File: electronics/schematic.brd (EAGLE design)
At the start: 100 x 80 mm, 3 parts, among them Q1 MC-405

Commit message: Board getting close. Before switching Around
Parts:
- removed SV1: (no value), con-lstb:MA06-1
- added GND, GND2, LED+, LED-, RST, RXD, TEST, TXD, VCC, VCC2: TPTP15R, testpad:TP15R
- added Q3: SST201, transistor-fet:SOT23
- moved Q1 1.91 mm to (22.9, 20.3)
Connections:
- removed net VSS: SV1.2, U$1.4
- new net GND: GND.TP, Q3.2, U$1.4
- new net N$4: LED-.TP, Q3.1
- net LED: now also Q3.3
- net N$1: now also Q1.P$6; no longer Q1.P$3
- net N$2: now also Q1.P$3; no longer Q1.P$6
- net RST: now also RST.TP; no longer SV1.1
- net RXD: now also RXD.TP; no longer SV1.6
- net TEST: now also TEST.TP; no longer SV1.4
- net TXD: now also TXD.TP; no longer SV1.5
- net VCC: now also LED+.TP, VCC.TP; no longer SV1.3
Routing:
- net VCC: track 7.39 -> 28.1 mm
- net VSS: track 10.4 -> 0.00 mm
- net GND: track 0.00 -> 8.23 mm
- net N$4: track 0.00 -> 4.15 mm
- net N$1: track 12.9 -> 11.4 mm
- net TXD: track 11.2 -> 9.93 mm
- net TEST: track 12.5 -> 11.2 mm
- net RST: track 12.9 -> 11.7 mm
- net RXD: track 11.7 -> 12.9 mm
- net N$2: track 9.47 -> 10.6 mm

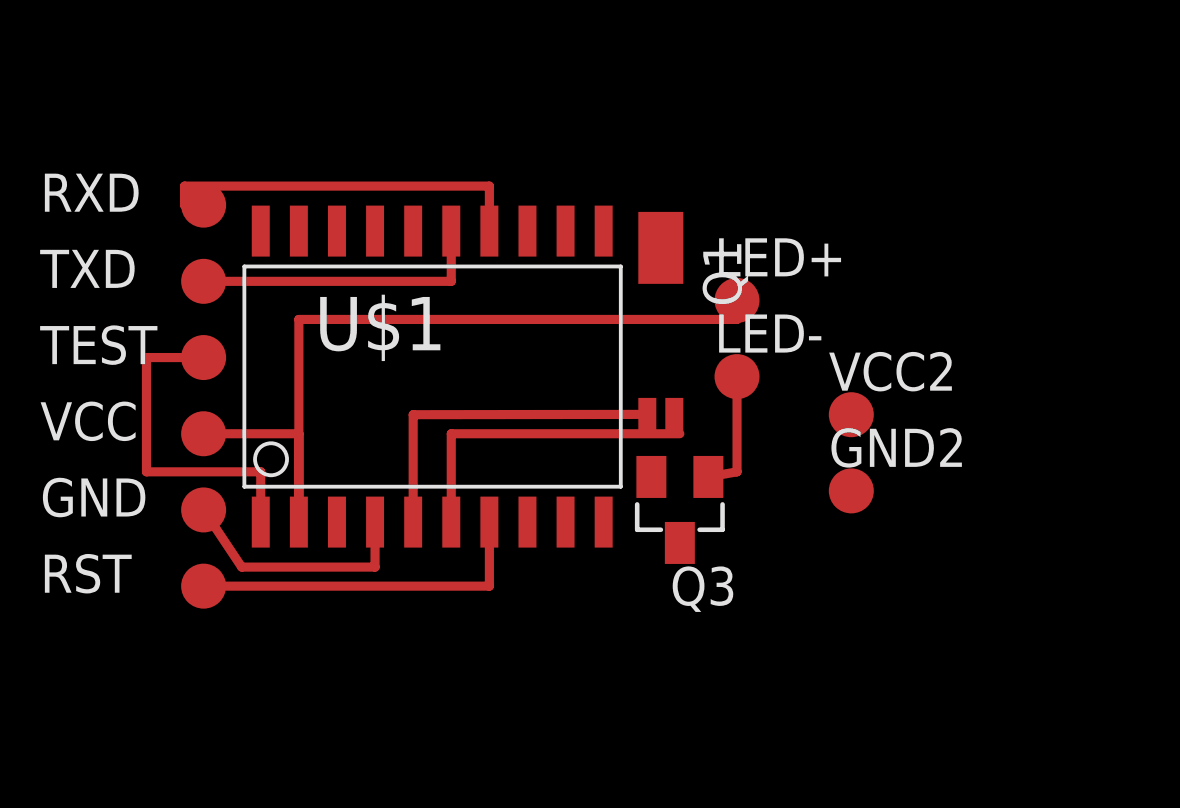
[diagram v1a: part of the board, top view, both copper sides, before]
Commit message: Finished 1 layer design
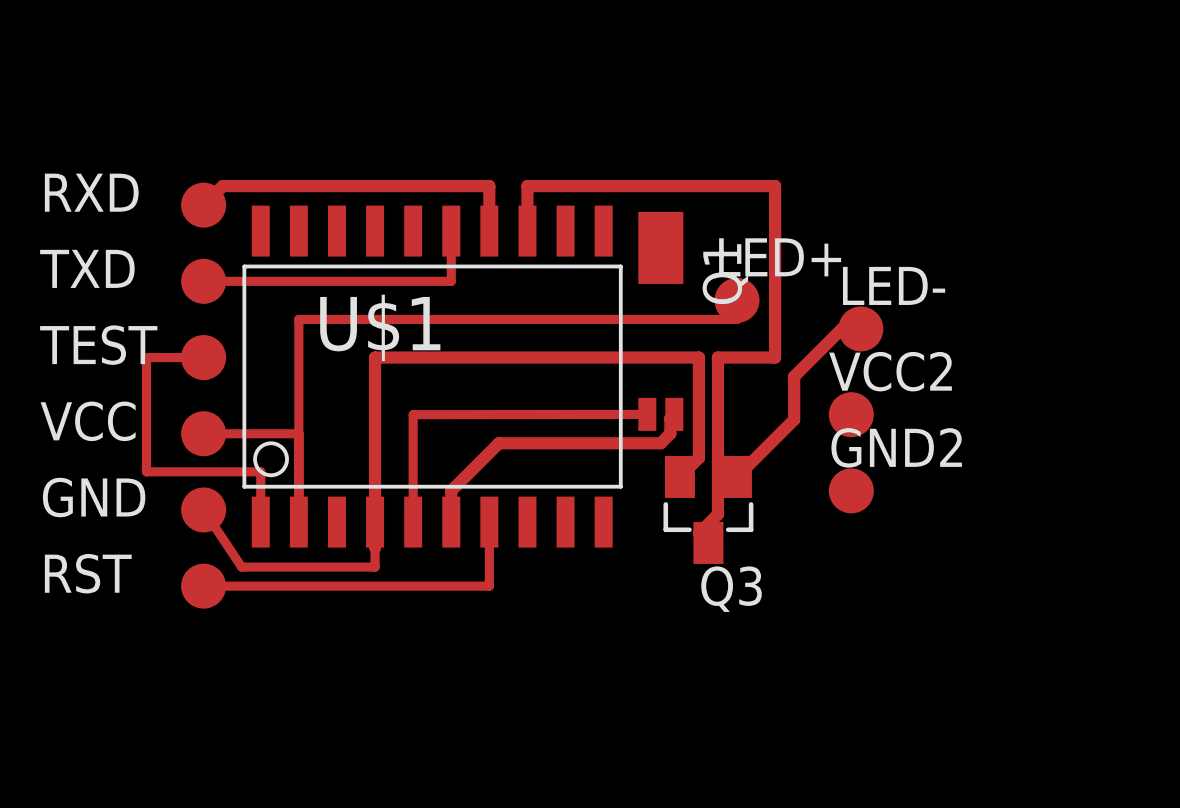
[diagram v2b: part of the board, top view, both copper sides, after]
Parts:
- moved LED- 4.42 mm to (29.5, 19.4)
- moved Q3 0.95 mm to (24.4, 13.3)
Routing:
- net LED: track 0.00 -> 23.9 mm
- net GND: track 8.23 -> 29.6 mm
- net N$4: track 4.15 -> 7.02 mm
- net RXD: track 12.9 -> 11.3 mm
- net N$2: track 10.6 -> 9.83 mm
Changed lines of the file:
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@@
 </element>
 <element name="U$1" library="TI_MSP430_v16" package="DW20" value="F21X1---DW20" x="15.24" y="17.78"/>
-<element name="Q3" library="transistor-fet" package="SOT23" value="SST201" x="23.495" y="13.335" rot="R180"/>
+<element name="Q3" library="transistor-fet" package="SOT23" value="SST201" x="24.4475" y="13.335" rot="R180"/>
 <element name="RXD" library="testpad" package="TP15R" value="TPTP15R" x="7.62" y="23.495" smashed="yes">
 <attribute name="TP_SIGNAL_NAME" value="" x="7.62" y="20.955" size="1" layer="37"/>
@@
 <attribute name="TP_SIGNAL_NAME" value="" x="25.4" y="20.32" size="1.778" layer="27" display="off"/>
 </element>
-<element name="LED-" library="testpad" package="TP15R" value="TPTP15R" x="25.4" y="17.78">
-<attribute name="TP_SIGNAL_NAME" value="" x="25.4" y="17.78" size="1.778" layer="27" display="off"/>
+<element name="LED-" library="testpad" package="TP15R" value="TPTP15R" x="29.5275" y="19.3675">
+<attribute name="TP_SIGNAL_NAME" value="" x="29.5275" y="19.3675" size="1.778" layer="27" display="off"/>
 </element>
 <element name="VCC2" library="testpad" package="TP15R" value="TPTP15R" x="29.21" y="16.51">
@@
 <contactref element="U$1" pad="6"/>
 <contactref element="Q1" pad="P$3"/>
-<wire x1="15.875" y1="12.93" x2="15.875" y2="15.875" width="0.3048" layer="1"/>
-<wire x1="15.875" y1="15.875" x2="23.495" y2="15.875" width="0.3048" layer="1"/>
-<wire x1="23.495" y1="15.875" x2="23.31" y2="16.52" width="0" layer="19" extent="1-16"/>
+<wire x1="23.31" y1="16.52" x2="23.1775" y2="16.3875" width="0.4064" layer="1"/>
+<wire x1="23.1775" y1="16.3875" x2="23.1775" y2="15.875" width="0.4064" layer="1"/>
+<wire x1="23.1775" y1="15.875" x2="22.86" y2="15.5575" width="0.4064" layer="1"/>
+<wire x1="22.86" y1="15.5575" x2="17.4625" y2="15.5575" width="0.4064" layer="1"/>
+<wire x1="17.4625" y1="15.5575" x2="15.875" y2="13.97" width="0.4064" layer="1"/>
+<wire x1="15.875" y1="13.97" x2="15.875" y2="12.93" width="0.4064" layer="1"/>
 </signal>
 <signal name="TEST">
@@
 <signal name="RXD">
 <contactref element="U$1" pad="14"/>
-<wire x1="17.145" y1="24.13" x2="17.145" y2="22.63" width="0" layer="19" extent="1-16"/>
 <contactref element="RXD" pad="TP"/>
-<wire x1="7.62" y1="23.495" x2="6.985" y2="23.495" width="0.3048" layer="1"/>
-<wire x1="6.985" y1="23.495" x2="6.985" y2="24.13" width="0.3048" layer="1"/>
-<wire x1="6.985" y1="24.13" x2="17.145" y2="24.13" width="0.3048" layer="1"/>
-<wire x1="17.145" y1="24.13" x2="17.145" y2="22.63" width="0.3048" layer="1"/>
+<wire x1="7.62" y1="23.495" x2="8.255" y2="24.13" width="0.4064" layer="1"/>
+<wire x1="8.255" y1="24.13" x2="17.145" y2="24.13" width="0.4064" layer="1"/>
+<wire x1="17.145" y1="24.13" x2="17.145" y2="22.63" width="0.4064" layer="1"/>
 </signal>
 <signal name="LED">
 <contactref element="U$1" pad="13"/>
 <contactref element="Q3" pad="3"/>
-<wire x1="23.495" y1="12.235" x2="18.415" y2="22.63" width="0" layer="19" extent="1-1"/>
+<wire x1="24.4475" y1="12.235" x2="24.13" y2="12.5525" width="0.4064" layer="1"/>
+<wire x1="26.67" y1="18.415" x2="26.67" y2="24.13" width="0.4064" layer="1"/>
+<wire x1="26.67" y1="24.13" x2="18.415" y2="24.13" width="0.4064" layer="1"/>
+<wire x1="18.415" y1="24.13" x2="18.415" y2="22.63" width="0.4064" layer="1"/>
+<wire x1="24.13" y1="12.5525" x2="24.765" y2="13.1875" width="0.4064" layer="1"/>
+<wire x1="24.765" y1="13.1875" x2="24.765" y2="18.415" width="0.4064" layer="1"/>
+<wire x1="24.765" y1="18.415" x2="26.67" y2="18.415" width="0.4064" layer="1"/>
 </signal>
 <signal name="GND">
@@
 <wire x1="7.62" y1="13.335" x2="8.89" y2="11.43" width="0.3048" layer="1"/>
 <wire x1="8.89" y1="11.43" x2="13.335" y2="11.43" width="0.3048" layer="1"/>
-<wire x1="13.335" y1="11.43" x2="13.335" y2="12.93" width="0.3048" layer="1"/>
-<wire x1="13.335" y1="12.93" x2="22.545" y2="14.435" width="0" layer="19" extent="1-1"/>
+<wire x1="13.335" y1="11.43" x2="13.335" y2="12.065" width="0.3048" layer="1"/>
+<wire x1="13.335" y1="12.065" x2="13.335" y2="12.93" width="0.3048" layer="1"/>
+<wire x1="23.4975" y1="14.435" x2="24.13" y2="15.0675" width="0.4064" layer="1"/>
+<wire x1="24.13" y1="15.0675" x2="24.13" y2="18.415" width="0.4064" layer="1"/>
+<wire x1="24.13" y1="18.415" x2="13.335" y2="18.415" width="0.4064" layer="1"/>
+<wire x1="13.335" y1="18.415" x2="13.335" y2="12.065" width="0.4064" layer="1"/>
 </signal>
 <signal name="N$4">
 <contactref element="Q3" pad="1"/>
 <contactref element="LED-" pad="TP"/>
-<wire x1="25.4" y1="17.78" x2="25.4" y2="14.605" width="0.3048" layer="1"/>
-<wire x1="25.4" y1="14.605" x2="24.445" y2="14.435" width="0.3048" layer="1"/>
+<wire x1="25.3975" y1="14.435" x2="27.305" y2="16.3425" width="0.4064" layer="1"/>
+<wire x1="27.305" y1="16.3425" x2="27.305" y2="17.78" width="0.4064" layer="1"/>
+<wire x1="27.305" y1="17.78" x2="28.8925" y2="19.3675" width="0.4064" layer="1"/>
+<wire x1="28.8925" y1="19.3675" x2="29.5275" y2="19.3675" width="0.4064" layer="1"/>
 </signal>
 </signals>

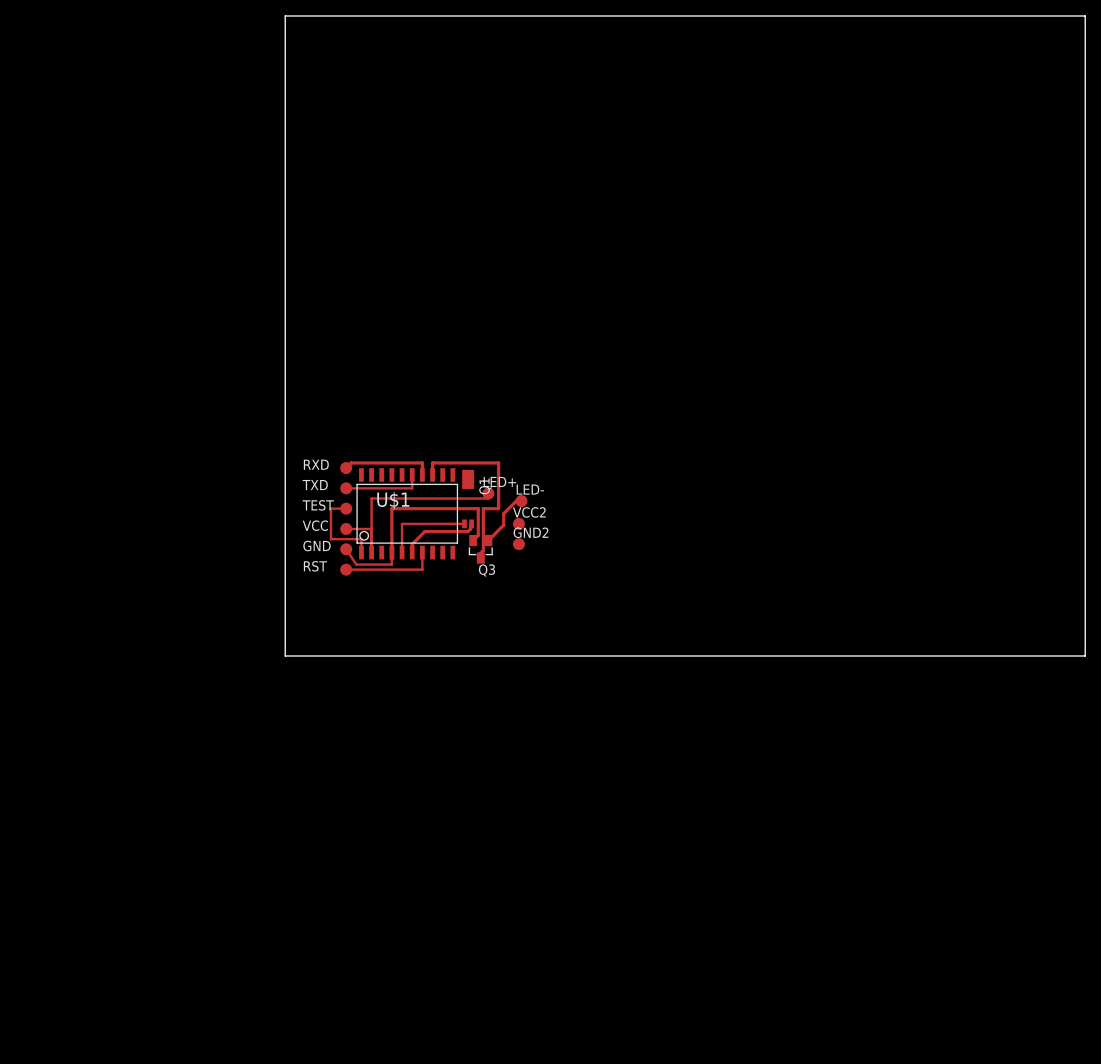
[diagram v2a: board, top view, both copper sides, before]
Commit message: Finished two layer design
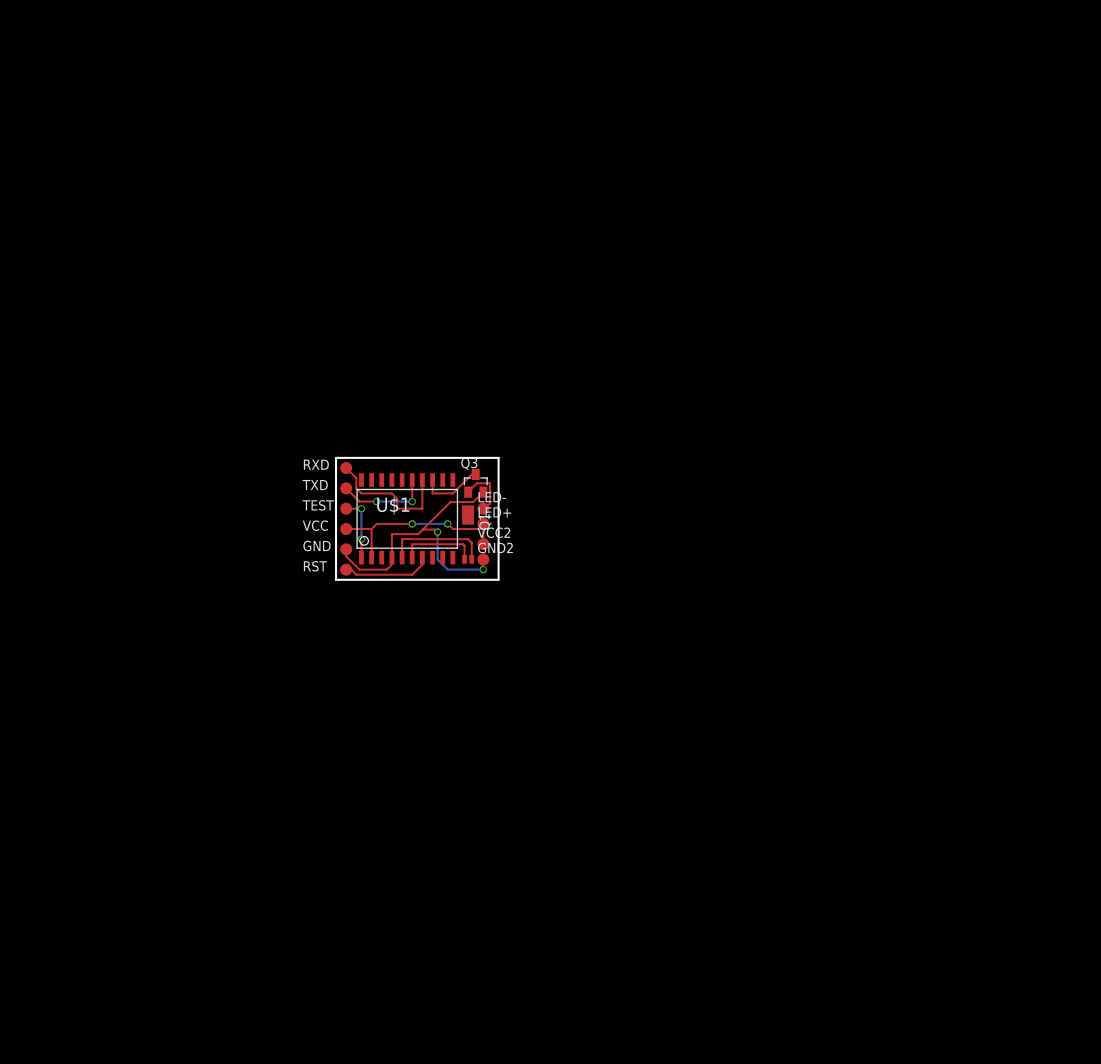
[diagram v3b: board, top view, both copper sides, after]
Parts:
- moved Q3 8.28 mm to (23.8, 21.6), turned to 0 degrees
- moved VCC2 5.12 mm to (24.8, 14.0)
- moved LED- 4.86 mm to (24.8, 18.4)
- moved GND2 4.84 mm to (24.8, 12.1)
- moved Q1 4.45 mm to (22.9, 15.9)
- moved LED+ 3.86 mm to (24.8, 16.5)
- moved U$1 0.64 mm to (15.2, 17.1)
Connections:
- net GND: now also GND2.TP
- net N$1: now also Q1.P$3; no longer Q1.P$6
- net N$2: now also Q1.P$6; no longer Q1.P$3
- net VCC: now also VCC2.TP
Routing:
- net LED: track 23.9 -> 8.05 mm
- net GND: track 29.6 -> 37.0 mm, vias 0 -> 2
- net RXD: track 11.3 -> 16.7 mm
- net VCC: track 28.1 -> 23.2 mm, vias 0 -> 2
- net TEST: track 11.2 -> 8.02 mm, vias 0 -> 2
- net N$1: track 11.4 -> 13.3 mm
- net TXD: track 9.93 -> 11.6 mm, vias 0 -> 2
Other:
- board size 100 x 80 mm -> 20.3 x 15.2 mm

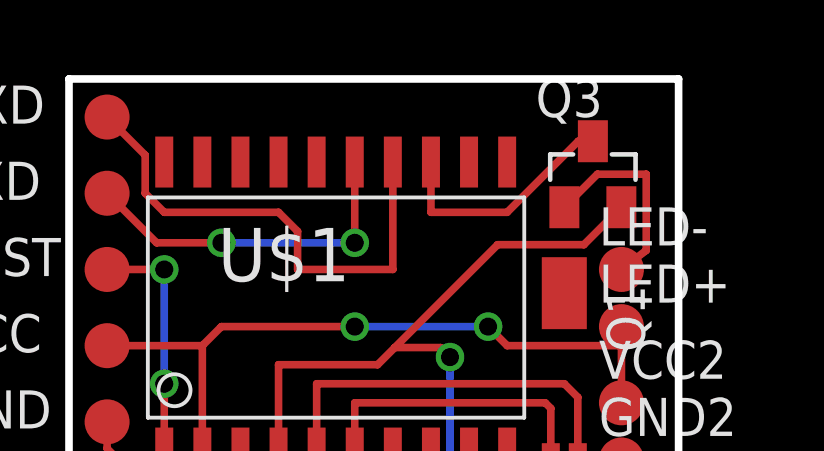
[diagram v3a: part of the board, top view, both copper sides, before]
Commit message: Added bypass capacitor
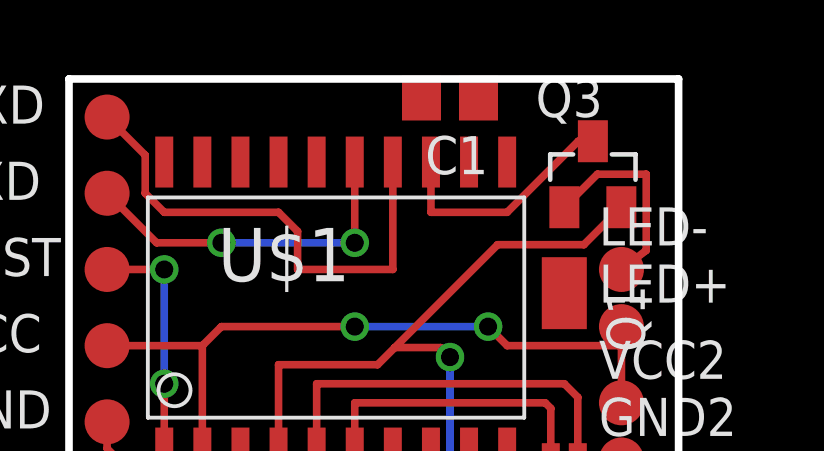
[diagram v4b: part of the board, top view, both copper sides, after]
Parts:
- added C1: (no value), resistor:C0805
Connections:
- net GND: now also C1.2
- net VCC: now also C1.1
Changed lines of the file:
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@@
 <attribute name="TP_SIGNAL_NAME" value="" x="24.765" y="12.065" size="1.778" layer="27" display="off"/>
 </element>
+<element name="C1" library="resistor" package="C0805" value="" x="19.05" y="24.13" rot="R180"/>
 </elements>
 <signals>
@@
 <contactref element="VCC2" pad="TP"/>
 <wire x1="24.765" y1="15.875" x2="24.765" y2="13.97" width="0.254" layer="1"/>
+<contactref element="C1" pad="1"/>
 <wire x1="24.765" y1="15.875" x2="24.765" y2="16.51" width="0" layer="19" extent="1-1"/>
+<wire x1="20" y1="24.13" x2="10.795" y2="12.295" width="0" layer="19" extent="1-1"/>
 </signal>
 <signal name="TXD">
@@
 <wire x1="19.05" y1="15.494" x2="18.7325" y2="15.8115" width="0.254" layer="1"/>
 <wire x1="18.7325" y1="15.8115" x2="17.2085" y2="15.8115" width="0.254" layer="1"/>
+<contactref element="C1" pad="2"/>
 <wire x1="13.335" y1="11.43" x2="13.335" y2="12.295" width="0" layer="19" extent="1-1"/>
+<wire x1="18.1" y1="24.13" x2="9.271" y2="10.795" width="0" layer="19" extent="1-1"/>
 </signal>
 <signal name="N$4">

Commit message: Very nice and finished
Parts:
- moved C1 13.3 mm to (22.9, 11.4), turned to 270 degrees
- moved Q1 1.91 mm to (22.9, 17.8)
- moved Q3 1.27 mm to (23.8, 22.9)
- moved GND2 0.90 mm to (25.4, 12.7)
- moved VCC2 0.90 mm to (25.4, 14.6)
- moved LED- 0.64 mm to (24.8, 19.1)
- moved LED+ 0.63 mm to (24.8, 17.1)
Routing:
- net GND: track 37.0 -> 45.3 mm
- net VCC: track 23.2 -> 26.9 mm
- net N$4: track 6.77 -> 3.66 mm
- net N$2: track 10.00 -> 8.48 mm
- net LED: track 8.05 -> 7.09 mm
- net N$1: track 13.3 -> 12.4 mm
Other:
- board size 20.3 x 15.2 mm -> 20.3 x 16.5 mm
